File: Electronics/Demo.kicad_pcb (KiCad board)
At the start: 2 copper layers, 61 x 49 mm, 27 parts, among them J1 RJ10, J2 RJ10, J3 Conn_01x02_Male, J4 PWR, SW1 SW_Push, SW2 SW_Push, SW3 SW_Push, U1 MCP2551-I-SN, U2 MCP2515-xSO, Y1 8MHz

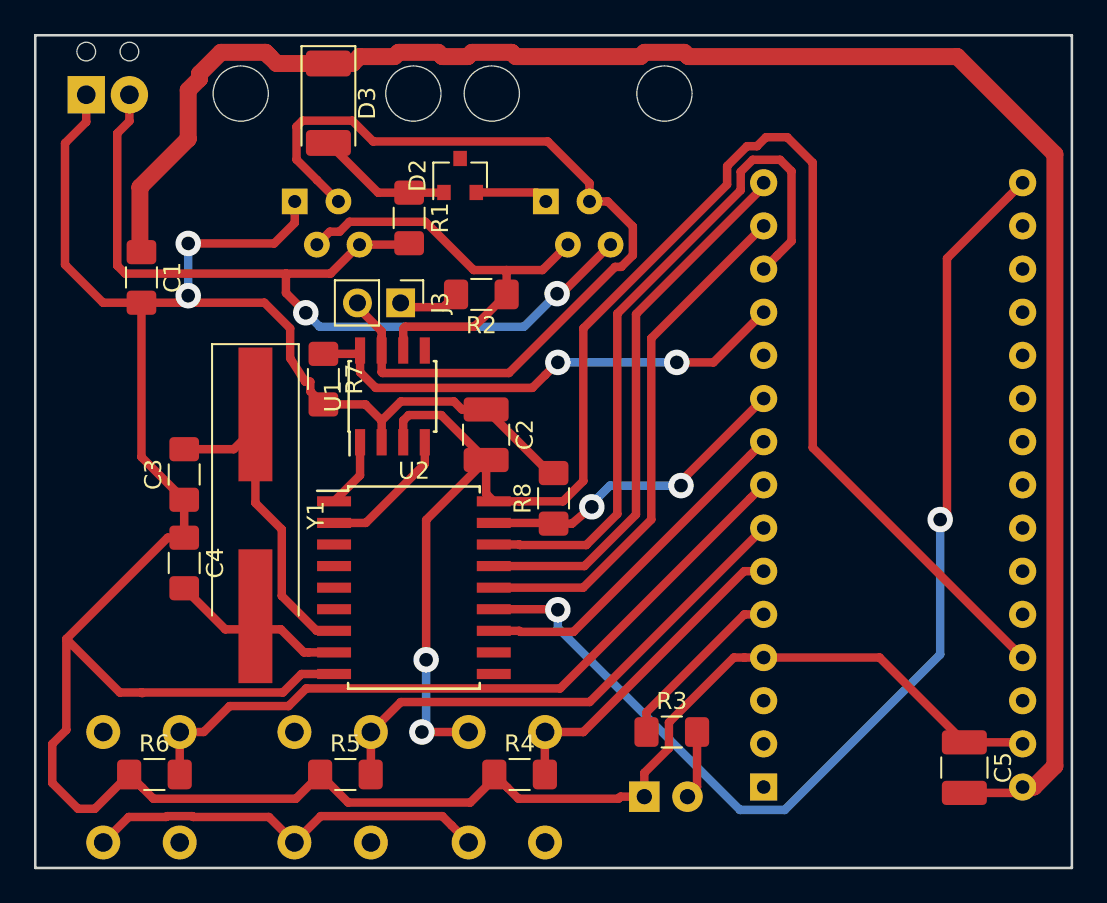
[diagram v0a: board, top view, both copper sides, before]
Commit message: Corrected footprint and tuned traces.
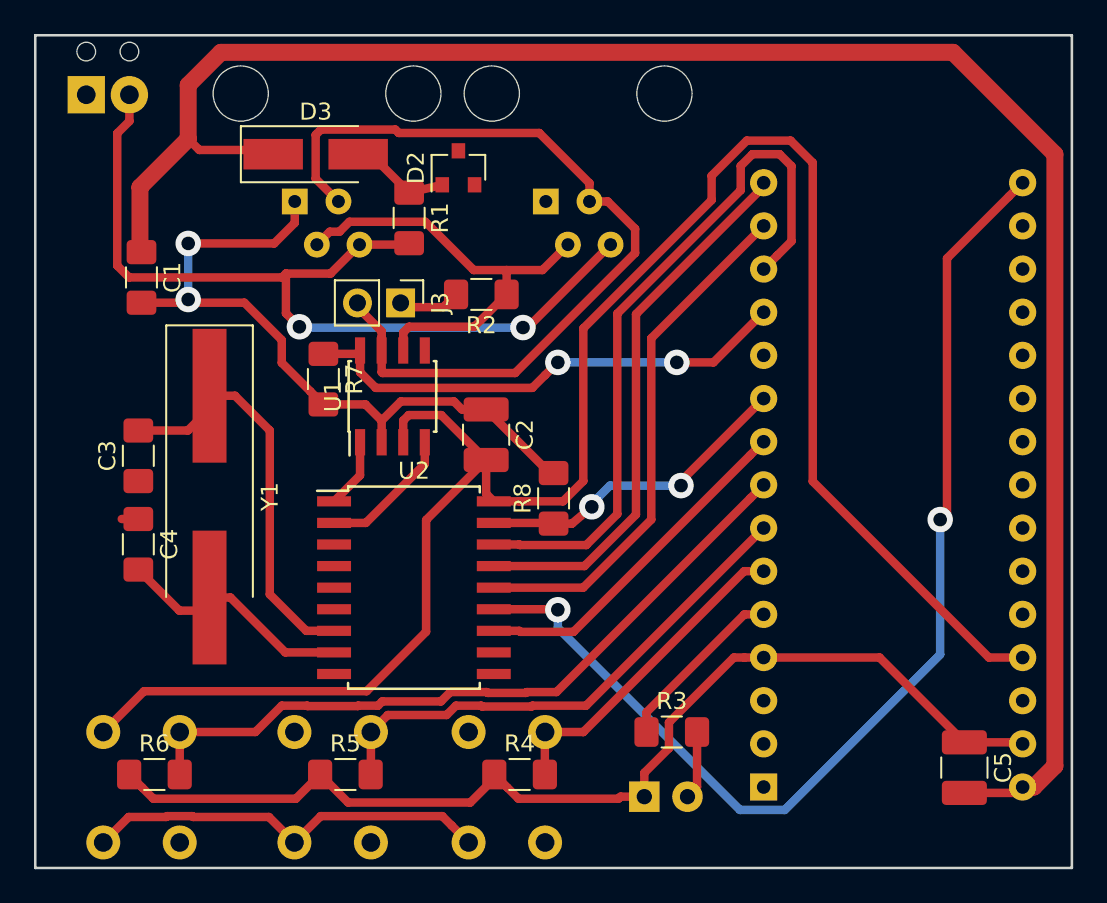
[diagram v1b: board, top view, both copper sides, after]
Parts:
- D3: footprint Diode_SMD:D_2010_5025Metric_Pad1.52x2.65mm_HandSolder -> Diode_SMD:D_SMA_Handsoldering
- moved D3 3.09 mm to (139.5, 89.0), turned to 0 degrees
- moved C3 2.92 mm to (129.1, 106.7)
- moved C4 2.92 mm to (129.1, 112.0)
- moved Y1 2.92 mm to (133.3, 109.2)
- moved D2 0.46 mm to (147.9, 89.8)
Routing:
- net GND: track 185.1 -> 108.5 mm
- net +5V: track 122.8 -> 136.7 mm, vias 2 -> 0
- net Net-(C3-Pad2): track 19.2 -> 23.4 mm
- net +12V: track 108.1 -> 112.1 mm
- net Net-(C4-Pad2): track 10.4 -> 13.9 mm
- net /CANH: track 52.9 -> 50.7 mm
- net Net-(D2-Pad1): track 8.02 -> 6.04 mm
- net /Vin: track 51.5 -> 52.5 mm
- net /CS: track 41.2 -> 41.8 mm
